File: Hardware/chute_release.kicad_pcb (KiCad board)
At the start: 4 copper layers, 20 x 35 mm, 60 parts, among them J1 Conn_01x03, J2 Conn_01x02_Pin, J3 USB4105-GF-A, Q1 DMG3415UFY4Q-7, Q2 SSM3K35AMFV_L3F, SW1 SH-7050TB, U1 W25Q128JVS, U2 RP2040, U3 AP7361C-33E, U4 MCP73831-2-OT, U5 DPS310XTSA1, Y1 ABM8-272-T3

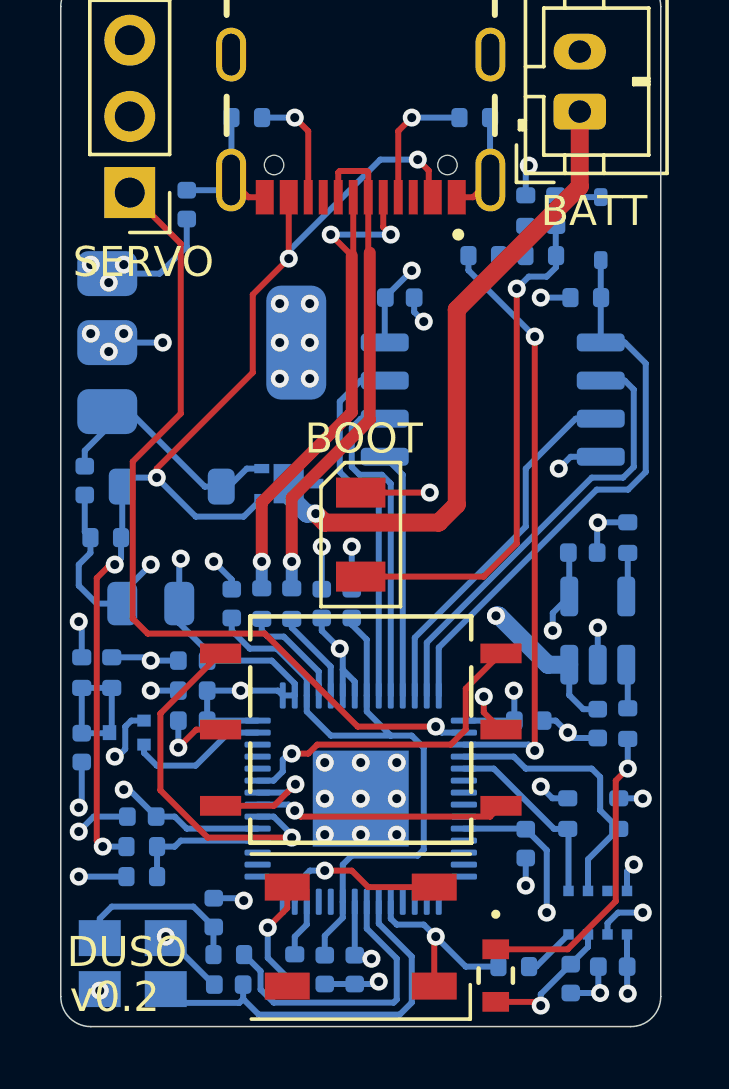
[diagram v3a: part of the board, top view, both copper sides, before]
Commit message: Updated silkscreen on pcb
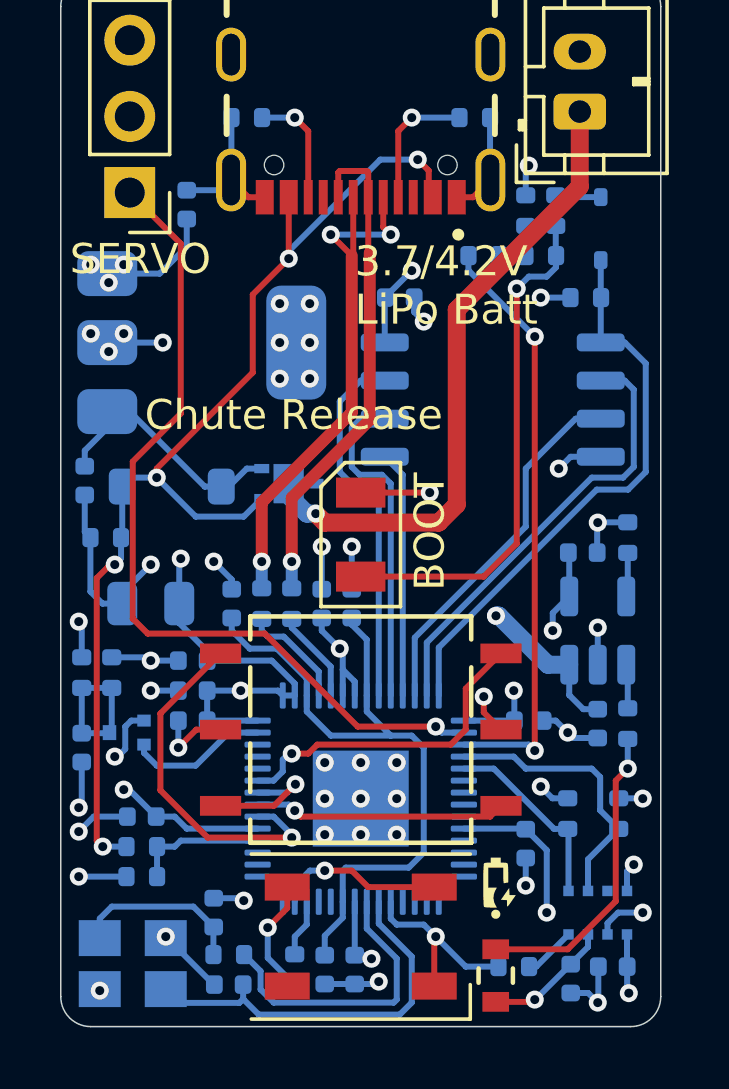
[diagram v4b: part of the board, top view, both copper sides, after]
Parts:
- added G***: LOGO, LOGO, F.Cu at (131.0, 111.8)
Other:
- rule pad_to_mask_clearance: 0.051 -> 0.038
- board text added: "3.7/4.2V LiPo Batt"
- board text added: "Chute Release"
- board text removed: "BATT"

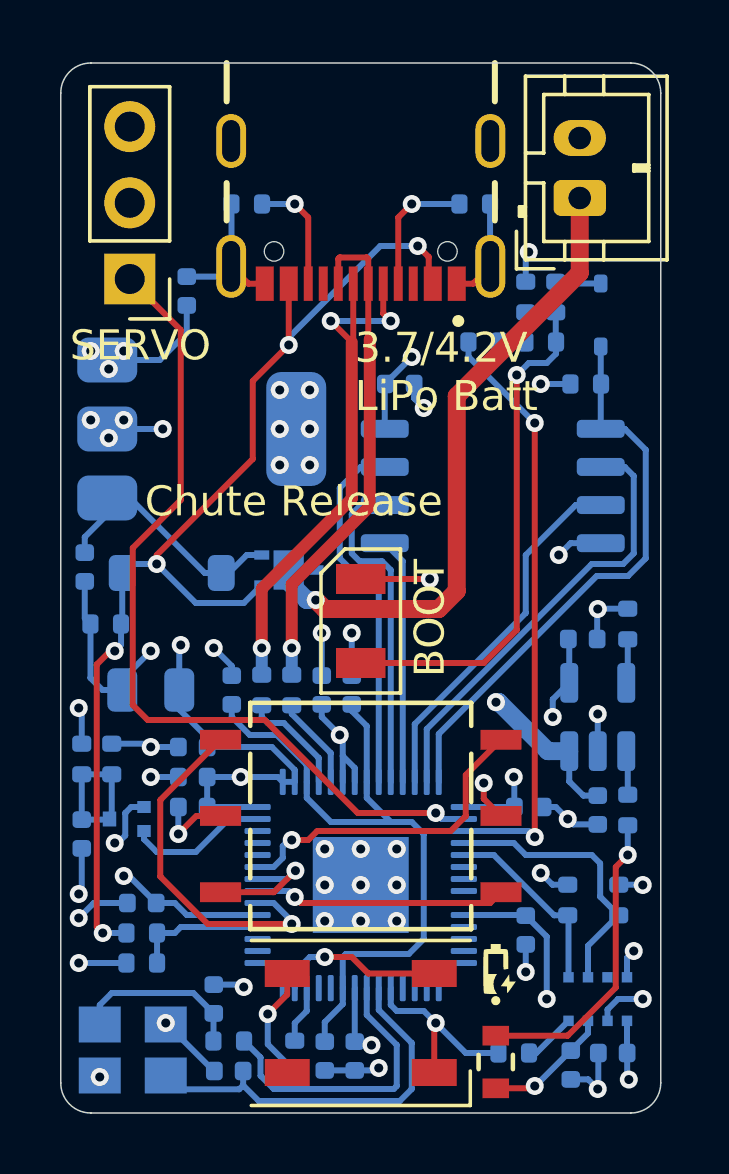
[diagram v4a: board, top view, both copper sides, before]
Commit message: Moved BOOT switch to bottom
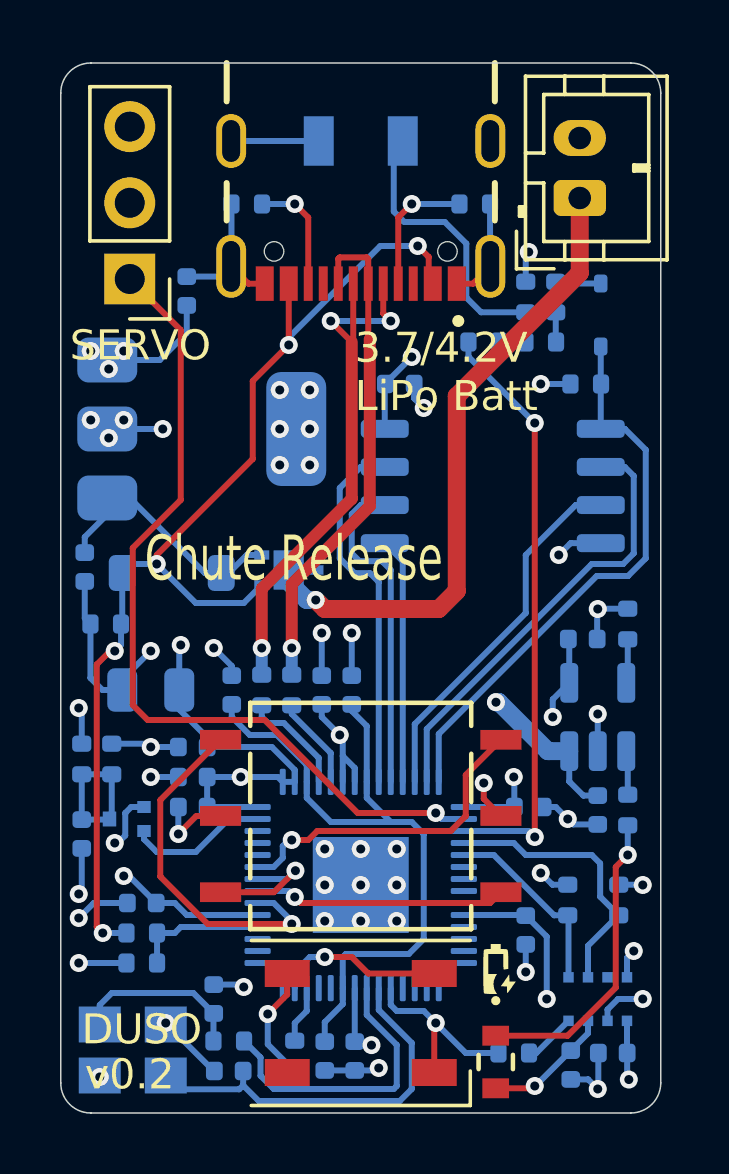
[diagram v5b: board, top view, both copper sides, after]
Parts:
- BOOT: moved to B.Cu
- moved BOOT 16.0 mm to (126.5, 84.2), turned to 0 degrees
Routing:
- net Net-(BOOT1-Pad2): track 18.1 -> 11.3 mm, vias 1 -> 0
- net GND: track 60.9 -> 61.5 mm, vias 45 -> 44

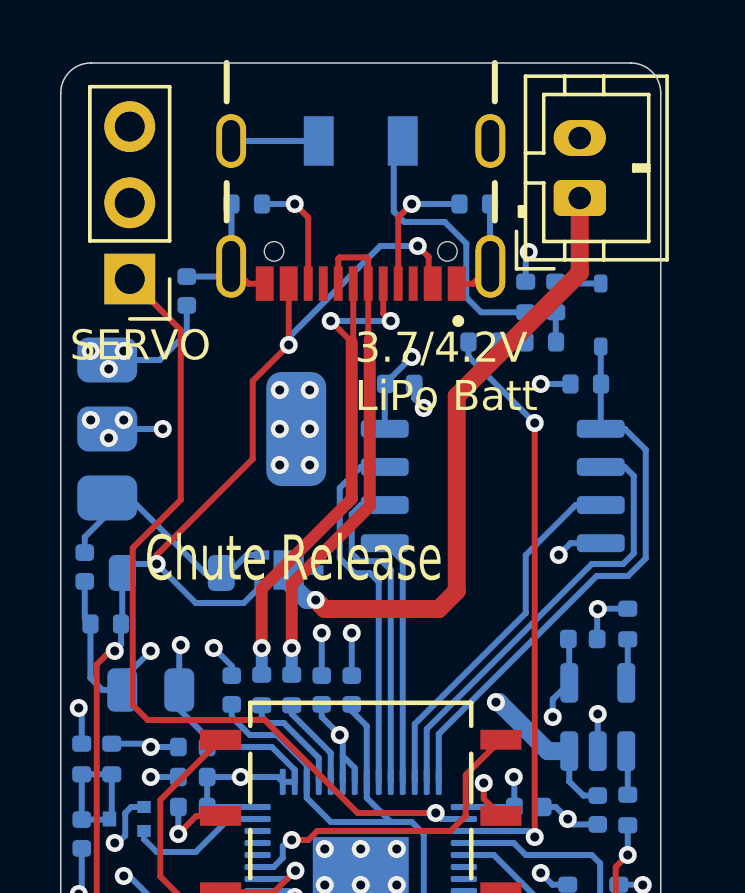
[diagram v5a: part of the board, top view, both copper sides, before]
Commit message: Added silkscreen for batt and servo polarity, and mode seletor switch
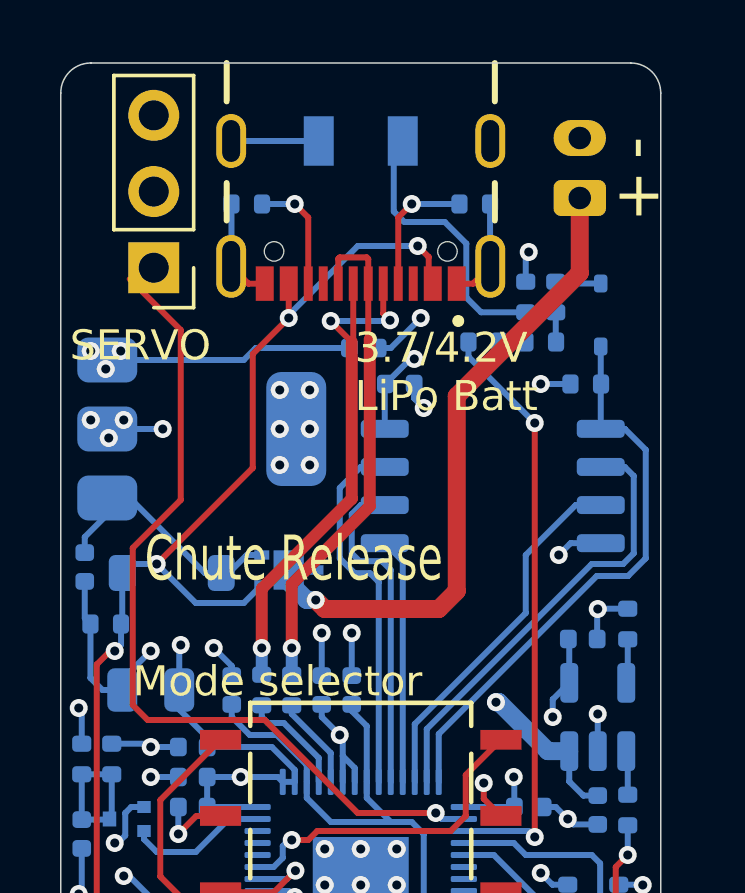
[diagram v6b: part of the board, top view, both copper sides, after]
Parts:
- moved C9 6.20 mm to (126.6, 91.1), turned to 0 degrees
- moved J1 0.88 mm to (119.6, 88.4)
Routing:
- net +3V3: track 58.4 -> 62.8 mm
- net GND: track 61.5 -> 61.8 mm, vias 44 -> 45
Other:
- board text added: "+"
- board text added: "-"
- board text added: "GND"
- board text added: "Mode selector"
- board text added: "SIG"

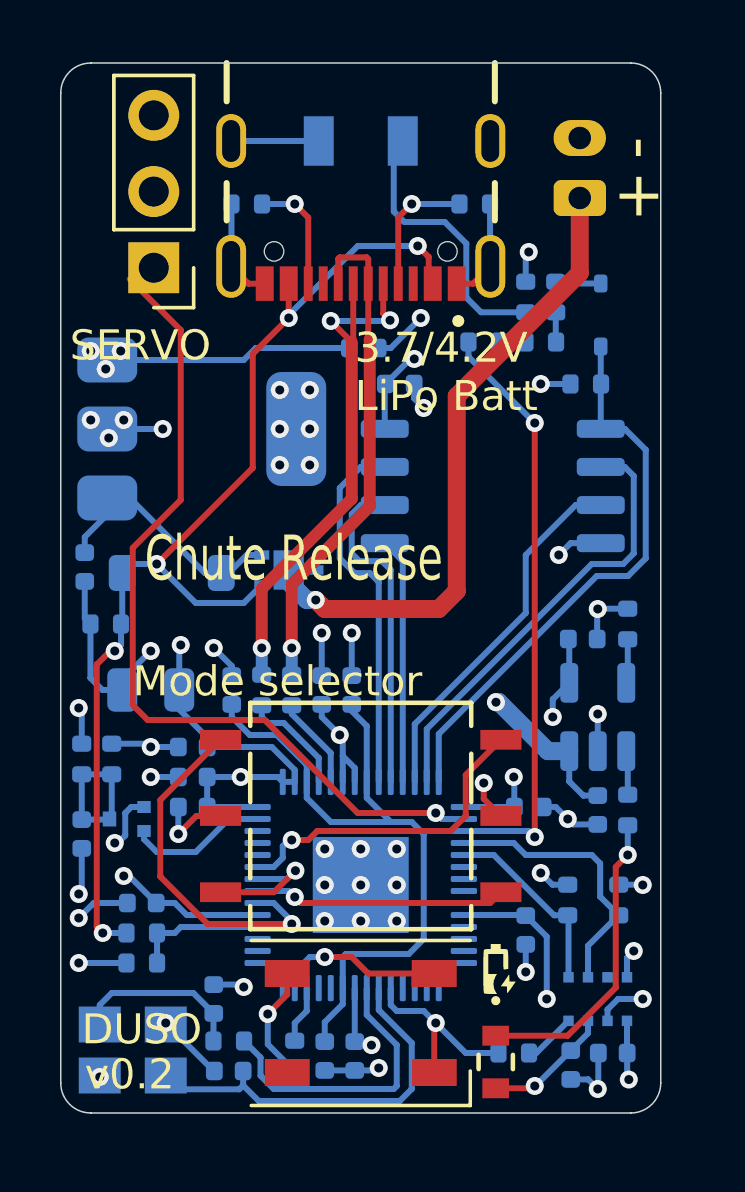
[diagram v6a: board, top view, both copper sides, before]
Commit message: Moved VBUS_DETECT from GPIO21 to GPIO19 to follow the rp2040 datasheet, updated some silkscreen
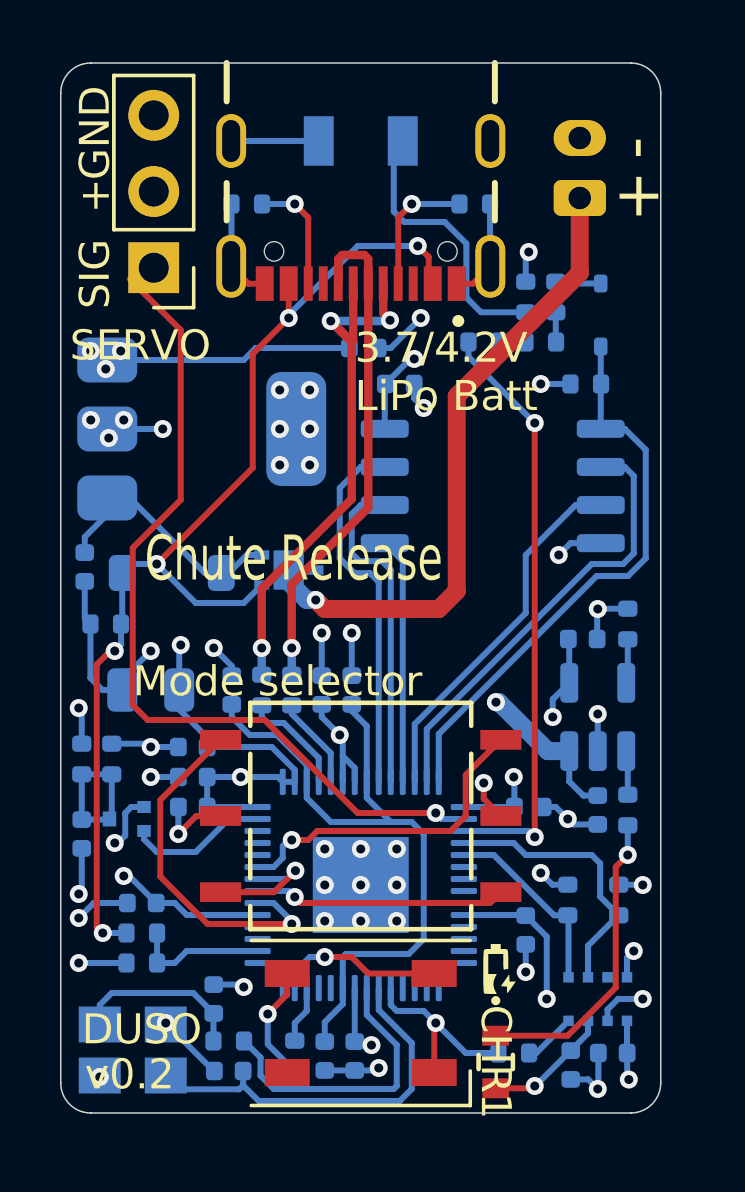
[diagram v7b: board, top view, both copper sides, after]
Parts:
- removed BOOT: SW_Push, duso:NanoT-AS
- added BOOT1: SW_Push, duso:NanoT-AS, B.Cu at (126.5, 84.2)
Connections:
- U2 pad 30: /MCU/GPIO19 -> VBUS_DETECT
- U2 pad 32: VBUS_DETECT -> /MCU/GPIO21
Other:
- board text added: "BOOT"

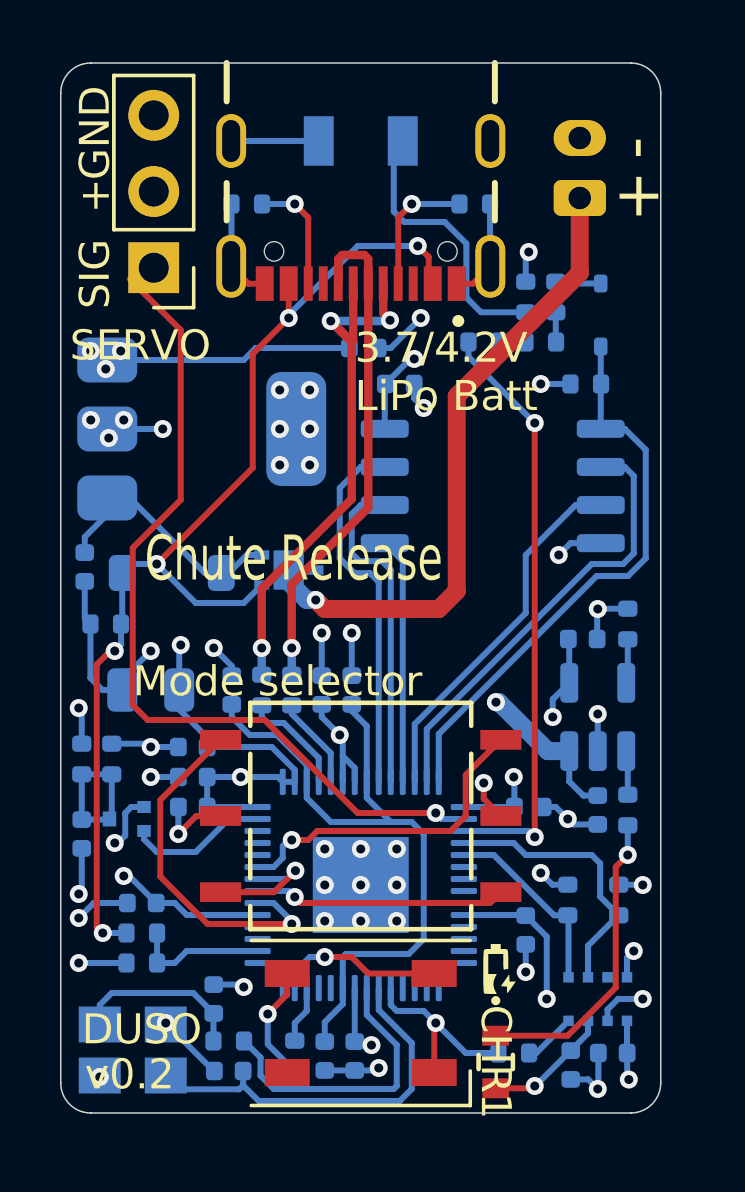
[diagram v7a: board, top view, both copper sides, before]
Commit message: Added external batt switch pin and bypass 0ohm res, changed ldo for smaller 600mA
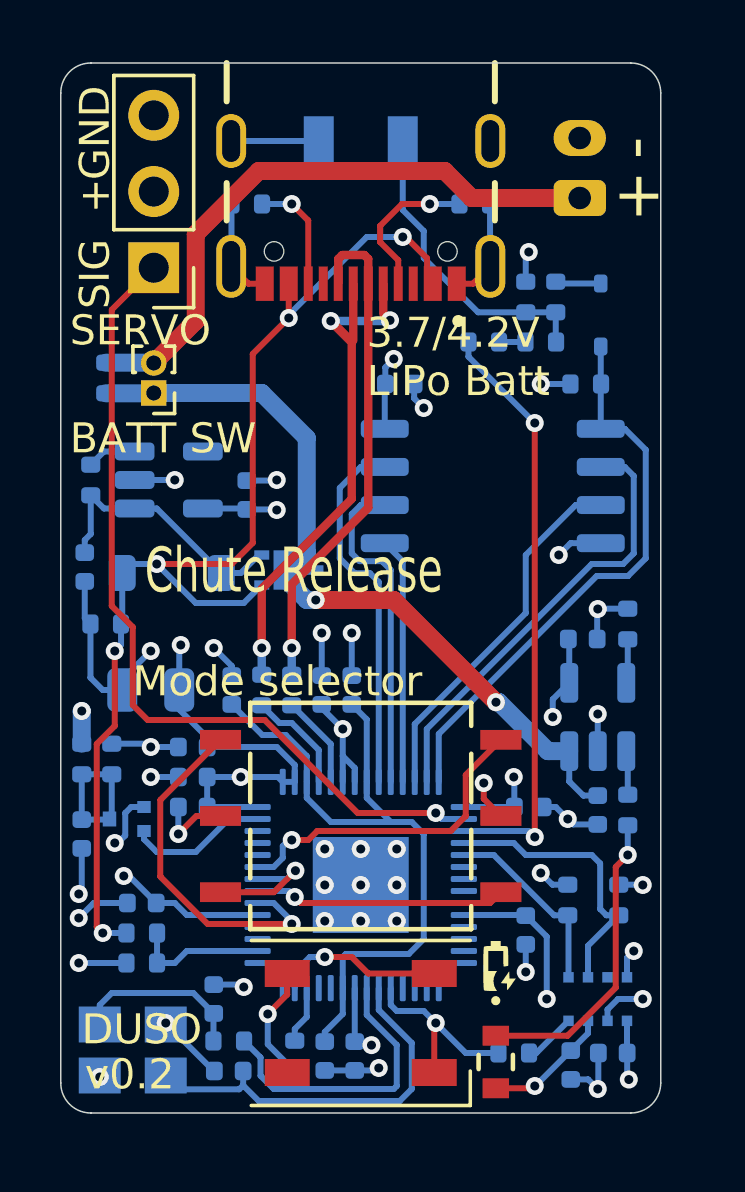
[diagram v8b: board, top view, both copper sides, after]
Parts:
- removed C9: 4.7u, Capacitor_SMD:C_0402_1005Metric
- added C23: 10u, Capacitor_SMD:C_0402_1005Metric, B.Cu at (122.7, 96.0)
- added J4: Conn_01x02, Connector_PinHeader_1.00mm:PinHeader_1x02_P1.00mm_Vertical, F.Cu at (119.6, 92.6)
- added R22: 10k, Resistor_SMD:R_0402_1005Metric, B.Cu at (117.5, 95.5)
- added R23: 0, Resistor_SMD:R_0402_1005Metric, B.Cu at (118.0, 92.1)
- C8: value 4.7u -> 1u
- U3: value AP7361C-33E -> AP2112K-3.3; footprint Package_TO_SOT_SMD:SOT-223-3_TabPin2 -> Package_TO_SOT_SMD:SOT-23-5
- moved U3 2.02 mm to (120.1, 95.5)
- moved G*** 0.10 mm to (131.0, 111.7)
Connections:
- J2 pad 1: +BATT -> Net-(J2-Pin_1)
- U3 pad 3: +3V3 -> Net-(U3-EN)
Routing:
- net Net-(J2-Pin_1): track 0.00 -> 20.5 mm
- net +3V3: track 62.8 -> 56.0 mm, vias 20 -> 18
- net GND: track 61.8 -> 59.7 mm, vias 45 -> 36
- net Net-(U3-EN): track 0.00 -> 1.64 mm
- net VBUS: track 36.9 -> 38.4 mm
- net Net-(BOOT1-Pad2): track 11.3 -> 10.3 mm
- net Net-(J3-CC1): track 4.43 -> 5.12 mm
- net +BATT: track 27.9 -> 27.3 mm
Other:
- board text added: "->"
- board text added: "BATT SW"
- board text added: "BATT SW BYPASS"
